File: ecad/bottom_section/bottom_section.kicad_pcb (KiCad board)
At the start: 2 copper layers, 4.3 x 3.6 mm, 53 parts, among them J1 JST PH, J2 JST SH, J3 JST PH, SW1 SW_Push, SW10 SW_Push, SW2 SW_Push, SW3 SW_Push, SW4 SW_Push, SW5 SW_Push, SW6 SW_Push, SW7 SW_Push, SW8 SW_Push, SW9 SW_Push, U1 MCP23017_ML

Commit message: Adds a bottom_section board.
It was fast. Seems the right design choices.
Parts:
- added REF**: MountingHole_2.7mm_M2.5, MountingHole:MountingHole_2.7mm_M2.5, F.Cu at (53.0, 55.5)
- added REF**: MountingHole_2.7mm_M2.5, MountingHole:MountingHole_2.7mm_M2.5, F.Cu at (147.0, 31.0)
- added REF**: MountingHole_2.7mm_M2.5, MountingHole:MountingHole_2.7mm_M2.5, F.Cu at (53.0, 31.0)
- added REF**: MountingHole_2.7mm_M2.5, MountingHole:MountingHole_2.7mm_M2.5, F.Cu at (147.0, 55.5)
- C11, J2, R1, R2, R3, R4, R5, R6, R7, R8, U1: moved to B.Cu
- J1, J3: footprint Connector_JST:JST_PH_S4B-PH-K_1x04_P2.00mm_Horizontal -> Connector_JST:JST_PH_S3B-PH-K_1x03_P2.00mm_Horizontal; moved to B.Cu
- moved C1 123.5 mm to (57.7, 47.3), turned to -90 degrees
- moved C2 123.5 mm to (76.8, 47.3), turned to -90 degrees
- moved C3 123.5 mm to (95.8, 47.3), turned to -90 degrees
- moved C4 123.5 mm to (114.8, 47.3), turned to -90 degrees
- moved C5 123.5 mm to (133.8, 47.3), turned to -90 degrees
- moved D10 122.9 mm to (141.5, 32.7), turned to 0 degrees
- moved D20 121.8 mm to (142.0, 61.7), turned to 0 degrees
- moved D4 118.3 mm to (89.3, 34.3)
- moved D6 118.3 mm to (108.3, 34.3)
- moved D8 118.3 mm to (127.3, 34.3)
- moved D2 118.3 mm to (70.2, 34.3)
- moved D3 118.3 mm to (81.0, 46.5), turned to 0 degrees
- moved D5 118.3 mm to (100.0, 46.5), turned to 0 degrees
- moved D7 118.3 mm to (119.0, 46.5), turned to 0 degrees
- moved D9 118.3 mm to (138.0, 46.5), turned to 0 degrees
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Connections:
- D11 pad 4: /KeyboardKey_COL6/DIN -> /KeyboardKey_COL1/DOUT
- D13 pad 2: /KeyboardKey_COL6/DIN -> /KeyboardKey_COL7/DOUT
- D13 pad 4: /KeyboardKey_COL7/DIN -> /KeyboardKey_COL6/DOUT
- D15 pad 2: /KeyboardKey_COL7/DIN -> /KeyboardKey_COL8/DOUT
- D15 pad 4: /KeyboardKey_COL8/DIN -> /KeyboardKey_COL7/DOUT
- D17 pad 2: /KeyboardKey_COL8/DIN -> /KeyboardKey_COL10/DIN
- D17 pad 4: /KeyboardKey_COL10/DOUT -> /KeyboardKey_COL8/DOUT
- D3 pad 2: /KeyboardKey_COL2/DOUT -> /KeyboardKey_COL1/DIN
- D3 pad 4: /KeyboardKey_COL1/DOUT -> /KeyboardKey_COL2/DIN
- D5 pad 2: /KeyboardKey_COL3/DOUT -> /KeyboardKey_COL2/DIN
- D5 pad 4: /KeyboardKey_COL2/DOUT -> /KeyboardKey_COL3/DIN
- D7 pad 2: /KeyboardKey_COL4/DOUT -> /KeyboardKey_COL3/DIN
- D7 pad 4: /KeyboardKey_COL3/DOUT -> /KeyboardKey_COL4/DIN
- D9 pad 2: /KeyboardKey_COL10/DIN -> /KeyboardKey_COL4/DIN
- D9 pad 4: /KeyboardKey_COL4/DOUT -> /KeyboardKey_COL5/DIN
- J1 pad 2: /SDIN -> /DIN
- J1 pad 3: /DIN -> +5V
- J3 pad 2: /SDOUT -> /DOUT
- J3 pad 3: /DOUT -> +5V
- R7 pad 1: /DIN -> /DOUT
- R7 pad 2: /KeyboardKey_COL1/DIN -> /KeyboardKey_COL10/DOUT
- R8 pad 1: /DOUT -> /DIN
- R8 pad 2: /KeyboardKey_COL6/DOUT -> /KeyboardKey_COL5/DIN
- U1 pad 17: /R5_SW -> /R6_SW
- U1 pad 18: /R6_S6 -> /R5_SW
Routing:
- net GND: track 0.00 -> 359.8 mm, vias 0 -> 29
- net +5V: track 0.00 -> 306.3 mm
- net /R5_SW: track 0.00 -> 95.1 mm, vias 0 -> 2
- net /COL5: track 0.00 -> 93.7 mm, vias 0 -> 3
- net /R6_SW: track 0.00 -> 78.0 mm
- net /COL4: track 0.00 -> 74.8 mm, vias 0 -> 3
- net /COL1: track 0.00 -> 59.1 mm, vias 0 -> 2
- net /COL3: track 0.00 -> 51.4 mm, vias 0 -> 3
- net /KeyboardKey_COL5/DIN: track 0.00 -> 49.9 mm
- net /COL2: track 0.00 -> 45.2 mm, vias 0 -> 3
- net /KeyboardKey_COL10/DOUT: track 0.00 -> 38.3 mm
- net /KeyboardKey_COL1/DOUT: track 0.00 -> 36.4 mm
- net /A2: track 0.00 -> 23.4 mm
- net /A1: track 0.00 -> 17.5 mm
- net +3V3: track 0.00 -> 17.3 mm
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- added copper zone on B.Cu, net GND
- added copper zone on F.Cu, net GND
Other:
- board size 4.3 x 3.6 mm -> 100 x 52 mm

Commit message: Updates boards
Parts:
- removed R2, R3, R4, R5, R6: 11k, Resistor_SMD:R_0603_1608Metric
- removed the REF** at (53.0, 55.5)
- added JP1: ~, Jumper:SolderJumper-3_P2.0mm_Open_TrianglePad1.0x1.5mm, F.Cu at (87.2, 56.0)
- added JP2: ~, Jumper:SolderJumper-3_P2.0mm_Open_TrianglePad1.0x1.5mm, F.Cu at (84.7, 56.0)
- added JP3: ~, Jumper:SolderJumper-3_P2.0mm_Open_TrianglePad1.0x1.5mm, F.Cu at (82.2, 56.0)
- added REF**: MountingHole_2.7mm_M2.5, MountingHole:MountingHole_2.7mm_M2.5, F.Cu at (53.0, 81.0)
- added REF**: MountingHole_2.7mm_M2.5, MountingHole:MountingHole_2.7mm_M2.5, F.Cu at (147.0, 81.0)
- J1, J3: value JST PH -> JST PH 3; footprint Connector_JST:JST_PH_S3B-PH-K_1x03_P2.00mm_Horizontal -> woodpecker:JST_PH_S3B-PH-SM4-TB_1x03-1MP_P2.00mm_Horizontal
- J2: value JST SH -> JST SH 4; footprint Connector_JST:JST_SH_BM04B-SRSS-TB_1x04-1MP_P1.00mm_Vertical -> woodpecker:JST_SH_BM04B-SRSS-TB_1x04-1MP_P1.00mm_Vertical
- moved REF** 40.5 mm to (106.5, 55.5)
- moved J1 10.6 mm to (95.1, 55.0)
- moved R8 7.32 mm to (101.0, 54.2), turned to 90 degrees
- moved R1 4.06 mm to (84.1, 53.9), turned to 90 degrees
- moved J3 3.58 mm to (132.8, 55.0)
- moved REF** 1.00 mm to (147.0, 30.0)
- moved REF** 1.00 mm to (53.0, 30.0)
- moved R7 0.51 mm to (126.9, 55.8)
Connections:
- R1 pad 2: /A2 -> /3v3_PUP
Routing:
- net +5V: track 306.3 -> 319.2 mm
- net /COL5: track 93.7 -> 106.0 mm
- net /KeyboardKey_COL5/DIN: track 49.9 -> 61.6 mm
- net GND: track 359.8 -> 350.2 mm, vias 29 -> 28
- net /3v3_PUP: track 0.00 -> 7.20 mm, vias 0 -> 1
- net /A0: track 15.5 -> 21.8 mm, vias 0 -> 1
- net /A2: track 23.4 -> 18.4 mm, vias 0 -> 1
- net +3V3: track 17.3 -> 13.5 mm
- net /A1: track 17.5 -> 19.8 mm, vias 0 -> 1
- net /COL4: track 74.8 -> 77.1 mm
- net /KeyboardKey_COL10/DOUT: track 38.3 -> 39.2 mm
- net /COL3: track 51.4 -> 52.0 mm
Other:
- board size 100 x 52 mm -> 100 x 57 mm
- board text added: "Addr"
- board text added: "↑ON"

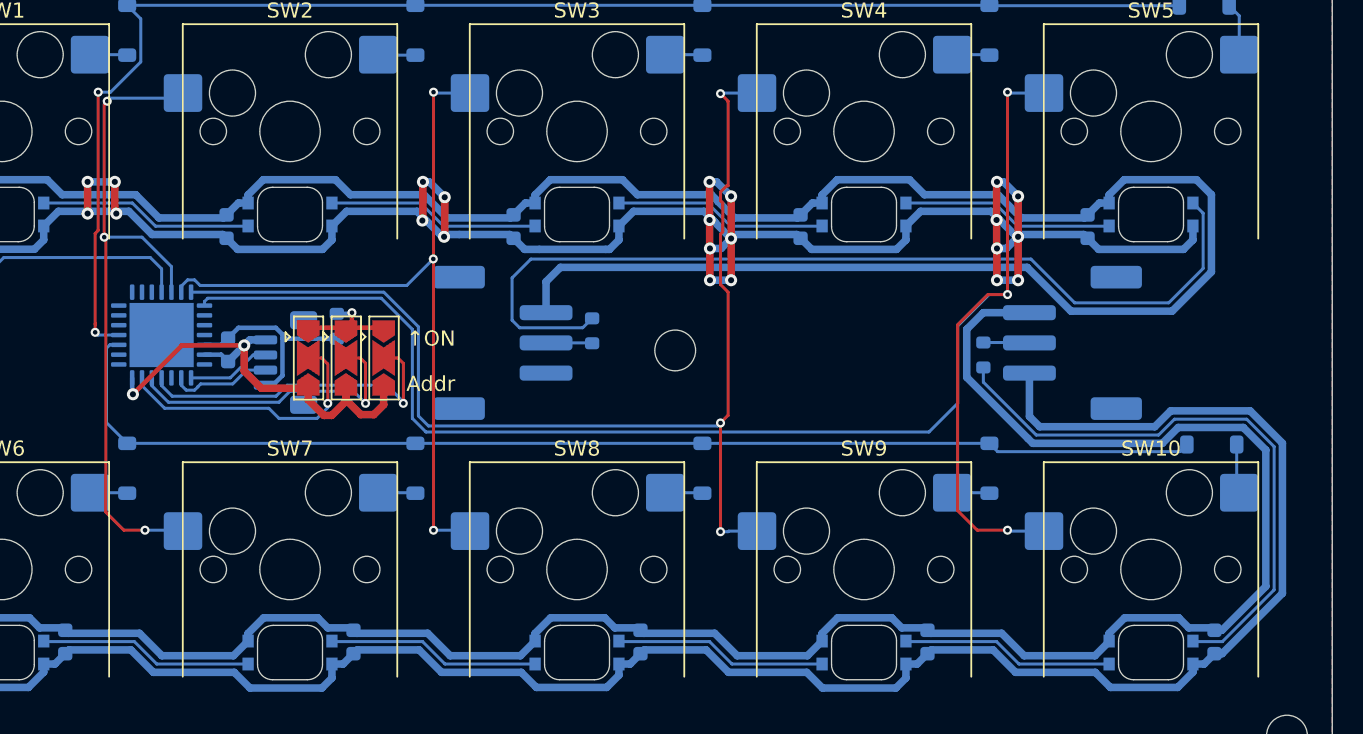
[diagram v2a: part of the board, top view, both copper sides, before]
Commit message: Uses Attiny1617 MCU for ADC & Matrix RO
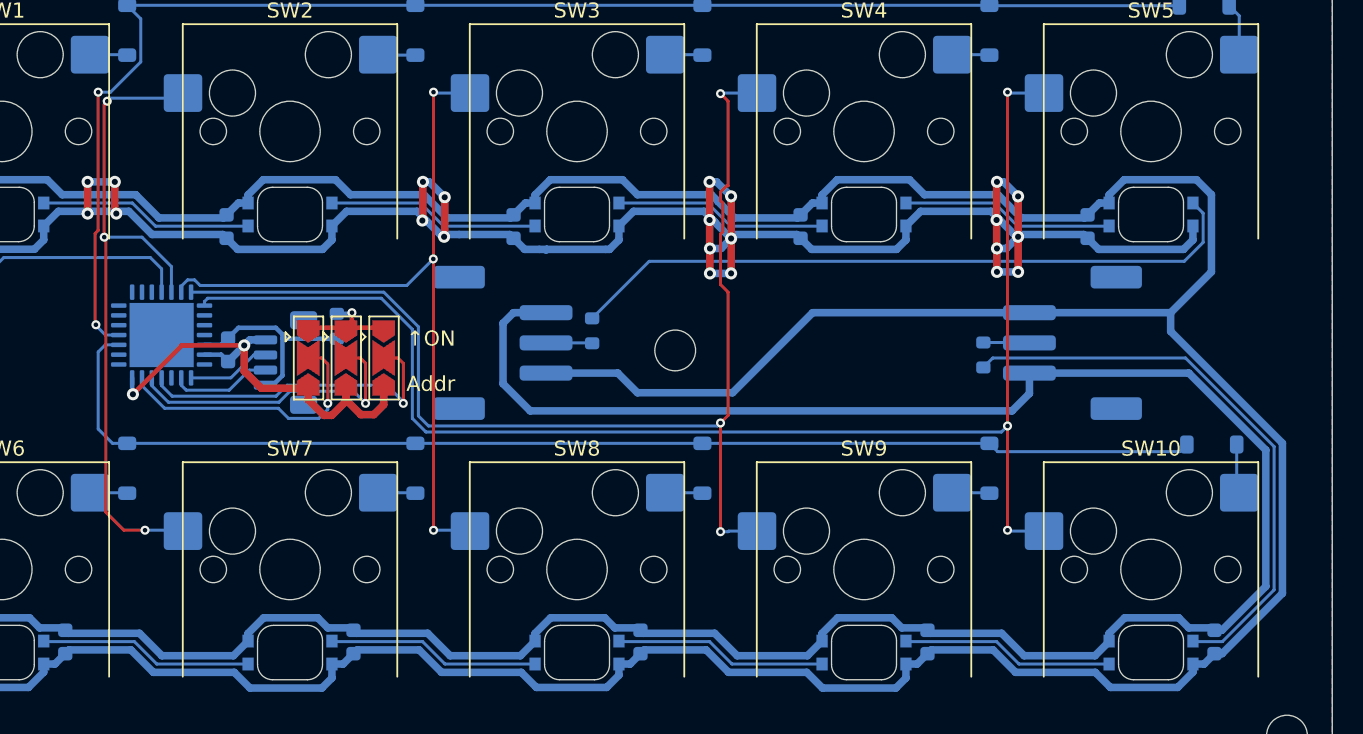
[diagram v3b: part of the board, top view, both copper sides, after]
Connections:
- J1 pad 1: GND -> +5V
- J1 pad 3: +5V -> GND
- J3 pad 1: GND -> +5V
- J3 pad 3: +5V -> GND
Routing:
- net GND: track 350.2 -> 380.1 mm
- net /KeyboardKey_COL5/DIN: track 61.6 -> 45.4 mm
- net /COL5: track 106.0 -> 94.7 mm
- net +5V: track 319.2 -> 308.8 mm
- net /R6_SW: track 78.3 -> 79.5 mm
- net /KeyboardKey_COL10/DOUT: track 39.2 -> 38.2 mm

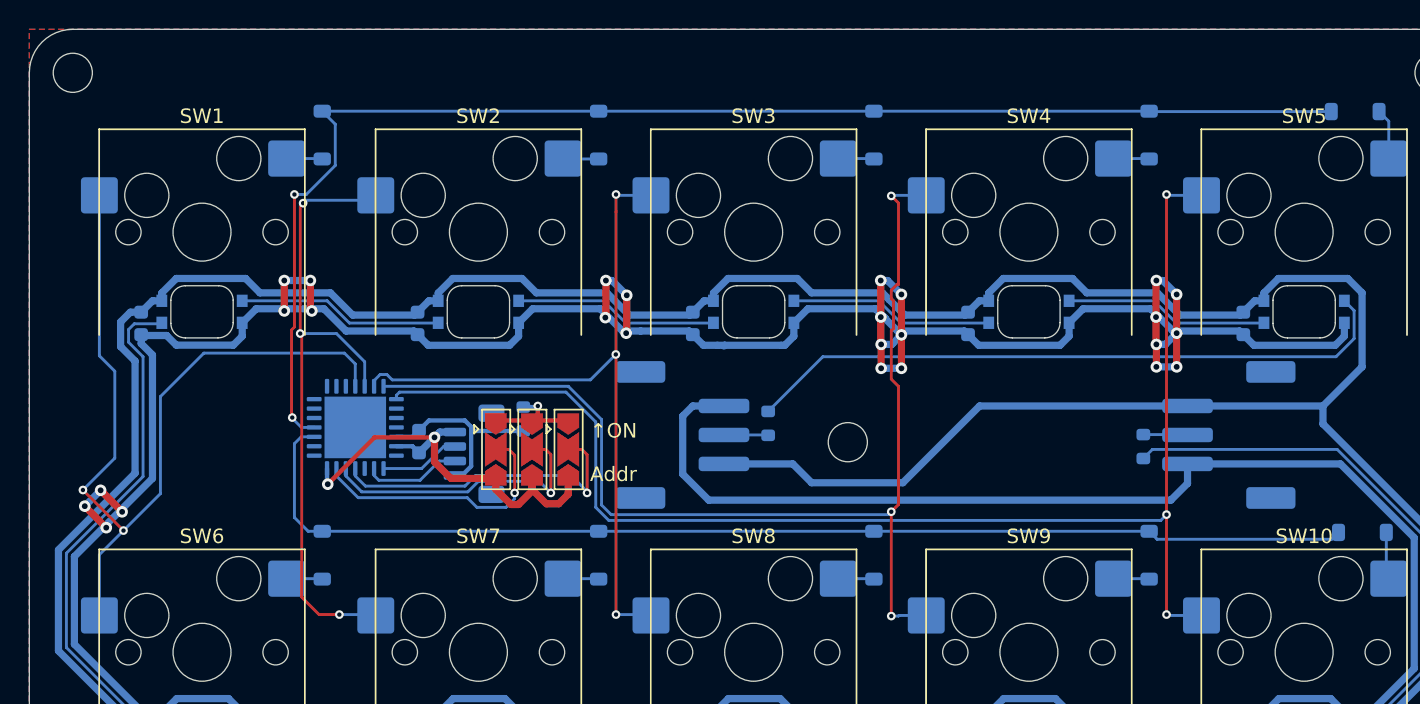
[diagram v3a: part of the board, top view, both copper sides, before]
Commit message: Uses attiny16176
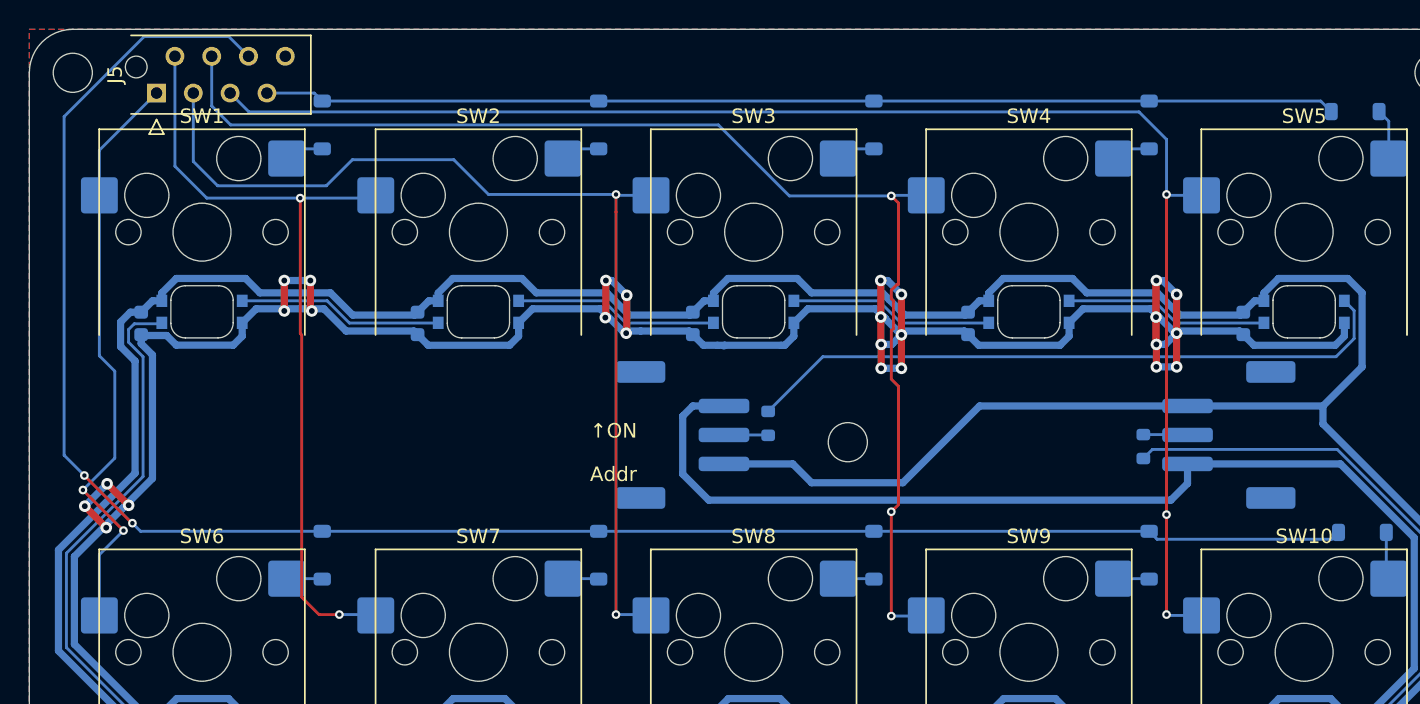
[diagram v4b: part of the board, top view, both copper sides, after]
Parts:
- removed C11: 100n, Capacitor_SMD:C_0603_1608Metric
- removed J2: JST SH 4, woodpecker:JST_SH_BM04B-SRSS-TB_1x04-1MP_P1.00mm_Vertical
- removed JP1, JP2, JP3: ~, Jumper:SolderJumper-3_P2.0mm_Open_TrianglePad1.0x1.5mm
- removed R1: 11k, Resistor_SMD:R_0603_1608Metric
- removed U1: MCP23017_ML, Package_DFN_QFN:QFN-28-1EP_6x6mm_P0.65mm_EP4.25x4.25mm
- added J5: Conn_01x08, Connector_TE-Connectivity:TE_Micro-MaTch_215079-8_2x04_P1.27mm_Vertical, F.Cu at (58.8, 31.4)
- moved D2 0.70 mm to (70.2, 33.6)
- moved D4 0.70 mm to (89.3, 33.6)
- moved D6 0.70 mm to (108.3, 33.6)
- moved D8 0.70 mm to (127.3, 33.6)
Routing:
- net /R6_SW: track 79.5 -> 129.5 mm, vias 0 -> 2
- net GND: track 380.1 -> 350.3 mm, vias 28 -> 26
- net /A0: track 21.8 -> 0.00 mm, vias 1 -> 0
- net /R5_SW: track 94.8 -> 74.0 mm, vias 2 -> 0
- net /A1: track 19.8 -> 0.00 mm, vias 1 -> 0
- net /A2: track 18.4 -> 0.00 mm, vias 1 -> 0
- net /COL3: track 52.0 -> 70.2 mm, vias 3 -> 2
- net /COL1: track 59.1 -> 40.9 mm
- net +3V3: track 13.5 -> 0.00 mm
- net /COL4: track 77.1 -> 87.8 mm
- net /COL2: track 45.2 -> 55.7 mm, vias 3 -> 2
- net /COL5: track 94.7 -> 103.6 mm
- net /3v3_PUP: track 7.20 -> 0.00 mm, vias 1 -> 0
- net /SDA: track 6.75 -> 0.00 mm
- net /SCK: track 5.55 -> 0.00 mm
